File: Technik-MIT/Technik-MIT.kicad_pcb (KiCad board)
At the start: 2 copper layers, 229 x 76.8 mm, 130 parts, among them J1 USB_C_Receptacle_USB2.0, SW1 SW_Push, SW10 SW_Push, SW11 SW_Push, SW12 SW_Push, SW13 SW_Push, SW14 SW_Push, SW15 SW_Push, SW16 SW_Push, SW17 SW_Push, SW18 SW_Push, SW19 SW_Push, SW2 SW_Push, SW20 SW_Push, SW21 SW_Push, SW22 SW_Push, SW23 SW_Push, SW24 SW_Push, SW25 SW_Push, SW26 SW_Push, SW27 SW_Push, SW28 SW_Push, SW29 SW_Push, SW3 SW_Push, SW30 SW_Push, SW31 SW_Push, SW32 SW_Push, SW33 SW_Push, SW34 SW_Push, SW35 SW_Push, SW36 SW_Push, SW37 SW_Push, SW38 SW_Push, SW39 SW_Push, SW4 SW_Push, SW40 SW_Push, SW41 SW_Push, SW42 SW_Push, SW43 SW_Push, SW44 SW_Push, SW45 SW_Push, SW46 SW_Push, SW47 SW_Push, SW48 RESET, SW5 SW_Push, SW6 SW_Push, SW7 SW_Push, SW8 SW_Push, SW9 SW_Push, U1 USBLC6-2SC6, U2 TVS0500DRV, U3 AP2127N-3.3, U4 W25Q32JVSS, U5 RP2040, Y1 Crystal_GND24

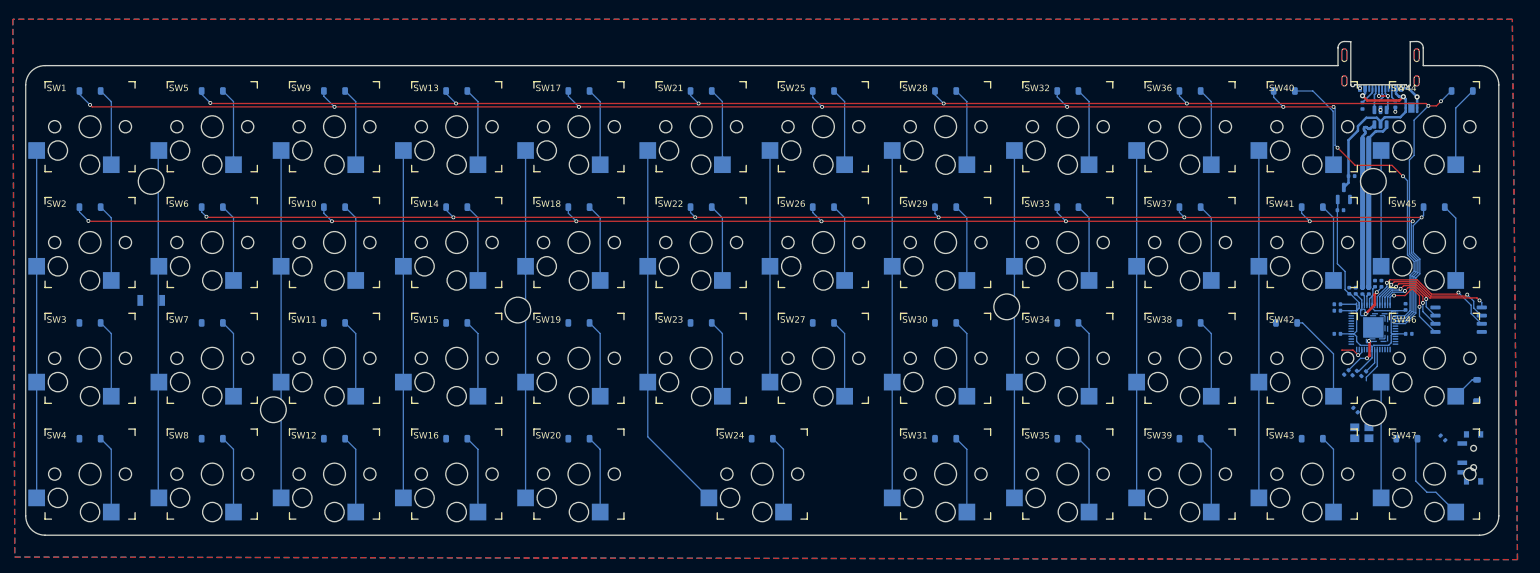
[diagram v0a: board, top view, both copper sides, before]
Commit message: Update PCB to match preexisting mounting holes
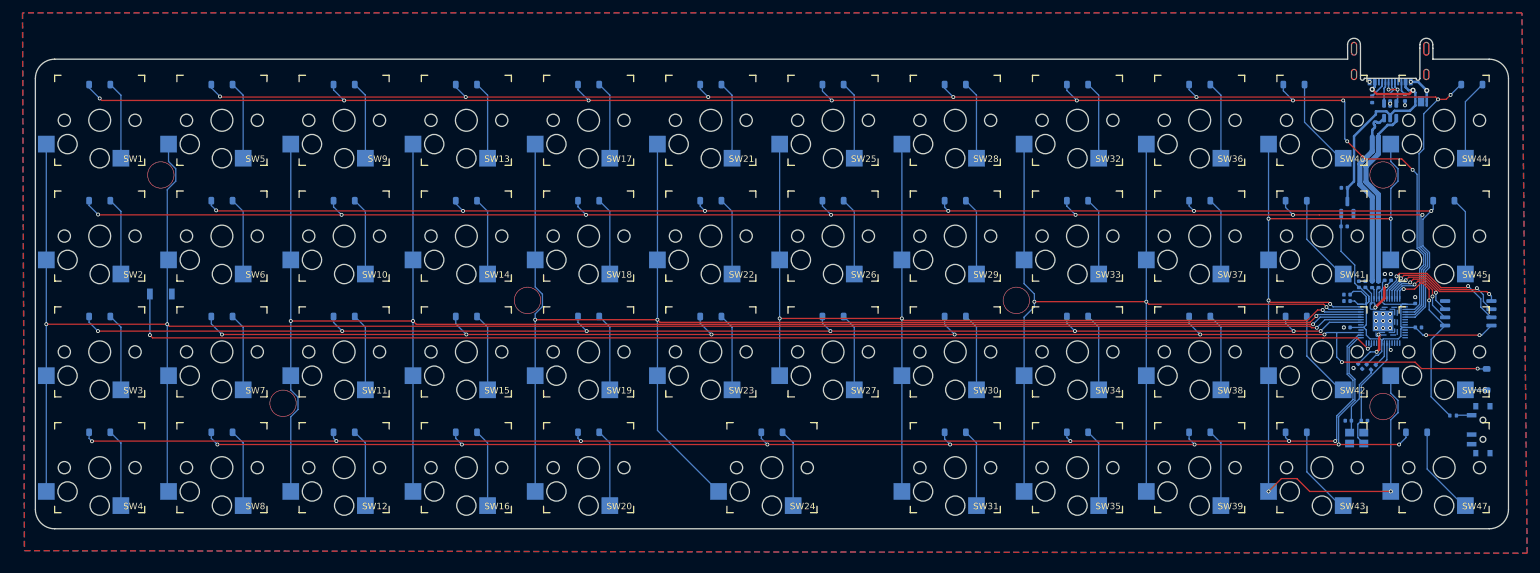
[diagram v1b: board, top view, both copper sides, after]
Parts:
- removed ? (x6): , 
- added H1: MountingHole_Pad, Technik-MIT:Standoff_Hole, F.Cu at (53.0, 58.5)
- added H2: MountingHole_Pad, Technik-MIT:Standoff_Hole, F.Cu at (72.0, 94.0)
- added H3: MountingHole_Pad, Technik-MIT:Standoff_Hole, F.Cu at (110.0, 78.0)
- added H4: MountingHole_Pad, Technik-MIT:Standoff_Hole, F.Cu at (186.0, 78.0)
- added H5: MountingHole_Pad, Technik-MIT:Standoff_Hole, F.Cu at (243.0, 58.5)
- added H6: MountingHole_Pad, Technik-MIT:Standoff_Hole, F.Cu at (243.0, 94.5)
- J1: footprint molex-216990_gct-usb45xx_hro-type-c-31-m-13x:Molex-216990_GCT-USB45xx_HRO-TYPE-C-31-M-13x -> Technik-MIT:Molex-216990_GCT-USB45xx_HRO-TYPE-C-31-M-13x
- moved DIP1 4.62 mm to (258.2, 98.1)
- moved R3 3.82 mm to (253.9, 95.9), turned to 180 degrees
- moved D41 2.69 mm to (229.5, 62.5)
- moved D43 2.69 mm to (229.5, 98.5)
- moved C2 2.59 mm to (236.9, 66.5)
- moved D46 2.27 mm to (259.1, 90.3), turned to -90 degrees
- moved U3 2.25 mm to (237.4, 63.6)
- moved C1 2.14 mm to (237.0, 60.5), turned to 180 degrees
- moved C12 2.12 mm to (237.4, 78.1)
- moved C14 2.12 mm to (237.4, 77.1)
- moved C5 2.00 mm to (237.6, 96.7), turned to 0 degrees
- moved U4 1.80 mm to (256.3, 80.0)
- moved C10 1.80 mm to (239.3, 75.5)
- moved C11 1.80 mm to (243.3, 74.4)
- moved C13 1.80 mm to (248.0, 78.0)
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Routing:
- net /ROW6: track 0.00 -> 222.5 mm, vias 0 -> 8
- net /ROW3: track 0.00 -> 220.3 mm, vias 0 -> 6
- net /ROW7: track 0.00 -> 216.4 mm, vias 0 -> 7
- net /ROW2: track 0.00 -> 213.8 mm, vias 0 -> 7
- net /COL0: track 108.1 -> 314.2 mm, vias 0 -> 3
- net Net-(U5-RUN): track 4.05 -> 197.8 mm, vias 1 -> 2
- net /COL1: track 108.0 -> 276.0 mm, vias 0 -> 3
- net /COL2: track 111.9 -> 241.9 mm, vias 0 -> 3
- net /COL3: track 90.0 -> 181.3 mm, vias 0 -> 3
- net /COL5: track 90.0 -> 146.3 mm, vias 0 -> 6
- net /COL4: track 108.0 -> 160.6 mm, vias 0 -> 3
- net /QSPI_SS: track 13.4 -> 29.6 mm
- net Net-(U5-XIN): track 5.57 -> 17.9 mm
- net +3V3: track 62.3 -> 73.5 mm, vias 0 -> 2
- net Net-(C5-Pad2): track 0.00 -> 11.2 mm
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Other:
- board size 229 x 76.8 mm -> 229 x 76.2 mm
- board text added: "Technik Drop-In Replacement Rev.1 by byungyoonc"

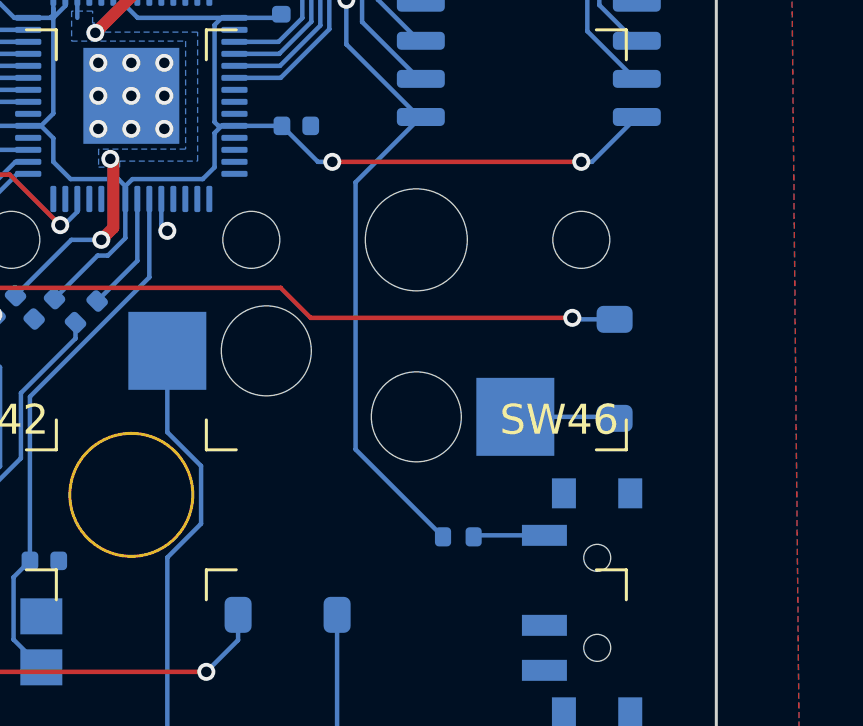
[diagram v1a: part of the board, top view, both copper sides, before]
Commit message: Update some of the silkscreen
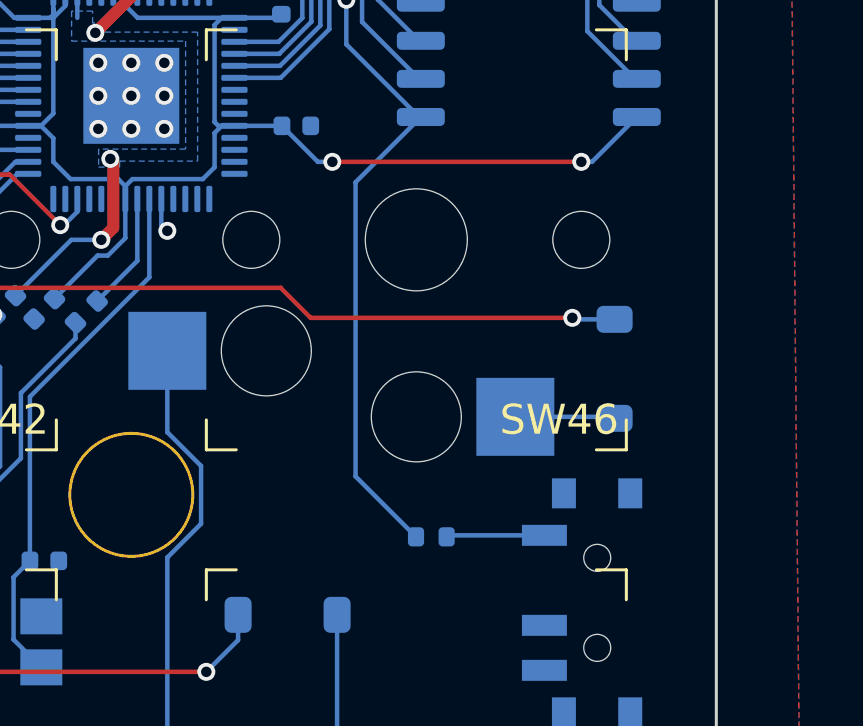
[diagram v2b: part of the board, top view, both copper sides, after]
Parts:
- moved R3 0.90 mm to (253.0, 95.9)
- renumbered DIP1 to BOOTSEL, SW48 to RESET
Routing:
- net Net-(DIP1-A): track 2.38 -> 3.28 mm
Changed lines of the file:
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@@
     (property "ki_keywords" "switch single-pole double-throw spdt ON-ON")
     (attr smd)
-    (fp_text reference "DIP1" (at 0 3.2 90) (layer "B.SilkS")
+    (fp_text reference "BOOTSEL" (at 0 3.2 90) (layer "B.SilkS")
         (effects (font (size 1 1) (thickness 0.15)) (justify mirror))
     )
@@
   )
   (footprint "Resistor_SMD:R_0402_1005Metric" (layer "B.Cu")
-    (at 253.9 95.9 180)
+    (at 253 95.9 180)
     (descr "Resistor SMD 0402 (1005 Metric), square (rectangular) end terminal, IPC_7351 nominal, (Body size source: IPC-SM-782 page 72, https://www.pcb-3d.com/wordpress/wp-content/uploads/ipc-sm-782a_amendment_1_and_2.pdf), generated with kicad-footprint-generator")
     (tags "resistor")
@@
     (property "ki_keywords" "switch normally-open pushbutton push-button")
     (attr smd)
-    (fp_text reference "SW48" (at 0 2.5) (layer "B.SilkS")
+    (fp_text reference "RESET" (at 0 2.5) (layer "B.SilkS")
         (effects (font (size 1 1) (thickness 0.15)) (justify mirror))
     )
@@
   (via (at 250.166797 77.997124) (size 0.6) (drill 0.35) (layers "F.Cu" "B.Cu") (net 67))
   (segment (start 250.166797 79.482022) (end 252.589775 81.905) (width 0.15) (layer "B.Cu") (net 67))
+  (segment (start 250.475 93.885) (end 252.49 95.9) (width 0.15) (layer "B.Cu") (net 67))
   (segment (start 245.874419 76.246901) (end 245.6 76.52132) (width 0.15) (layer "B.Cu") (net 67))
   (segment (start 252.650105 81.905) (end 250.475 84.080105) (width 0.15) (layer "B.Cu") (net 67))
+  (segment (start 250.475 84.080105) (end 250.475 93.885) (width 0.15) (layer "B.Cu") (net 67))
   (segment (start 246.208667 76.246901) (end 245.874419 76.246901) (width 0.15) (layer "B.Cu") (net 67))
   (segment (start 245.6 76.52132) (end 245.6 77.7625) (width 0.15) (layer "B.Cu") (net 67))
   (segment (start 252.589775 81.905) (end 252.650105 81.905) (width 0.15) (layer "B.Cu") (net 67))
-  (segment (start 250.475 84.080105) (end 250.475 92.985) (width 0.15) (layer "B.Cu") (net 67))
   (segment (start 250.166797 77.997124) (end 250.166797 79.482022) (width 0.15) (layer "B.Cu") (net 67))
-  (segment (start 250.475 92.985) (end 253.448751 95.958751) (width 0.15) (layer "B.Cu") (net 67))
   (segment (start 243.731558 50.725) (end 242.275022 52.181536) (width 0.4) (layer "B.Cu") (net 68))
   (segment (start 242.274999 55.225001) (end 242.274999 52.57033) (width 0.8) (layer "B.Cu") (net 68))
@@
   (segment (start 243.6 76.4) (end 243.6 77.7625) (width 0.15) (layer "B.Cu") (net 84))
   (segment (start 245.093626 74.906374) (end 243.6 76.4) (width 0.15) (layer "B.Cu") (net 84))
-  (segment (start 254.46 95.85) (end 254.41 95.9) (width 0.15) (layer "B.Cu") (net 95))
-  (segment (start 256.77 95.85) (end 254.46 95.85) (width 0.15) (layer "B.Cu") (net 95))
+  (segment (start 256.77 95.85) (end 253.56 95.85) (width 0.15) (layer "B.Cu") (net 95))
+  (segment (start 253.56 95.85) (end 253.51 95.9) (width 0.15) (layer "B.Cu") (net 95))
   (segment (start 179.8 46.09375) (end 178.15 44.44375) (width 0.15) (layer "B.Cu") (net 104))
   (segment (start 179.8 55.9) (end 179.8 46.09375) (width 0.15) (layer "B.Cu") (net 104))
